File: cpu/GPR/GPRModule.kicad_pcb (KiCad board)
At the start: 2 copper layers, 100 x 80 mm, 52 parts, among them J1 Interconnect, U1 74HCT574, U10 74LS245, U11 74LS126, U2 74HCT574, U3 74LS245, U4 74LS245, U5 74LS245, U6 74LS245, U7 74LS245, U8 74LS245, U9 74LS245

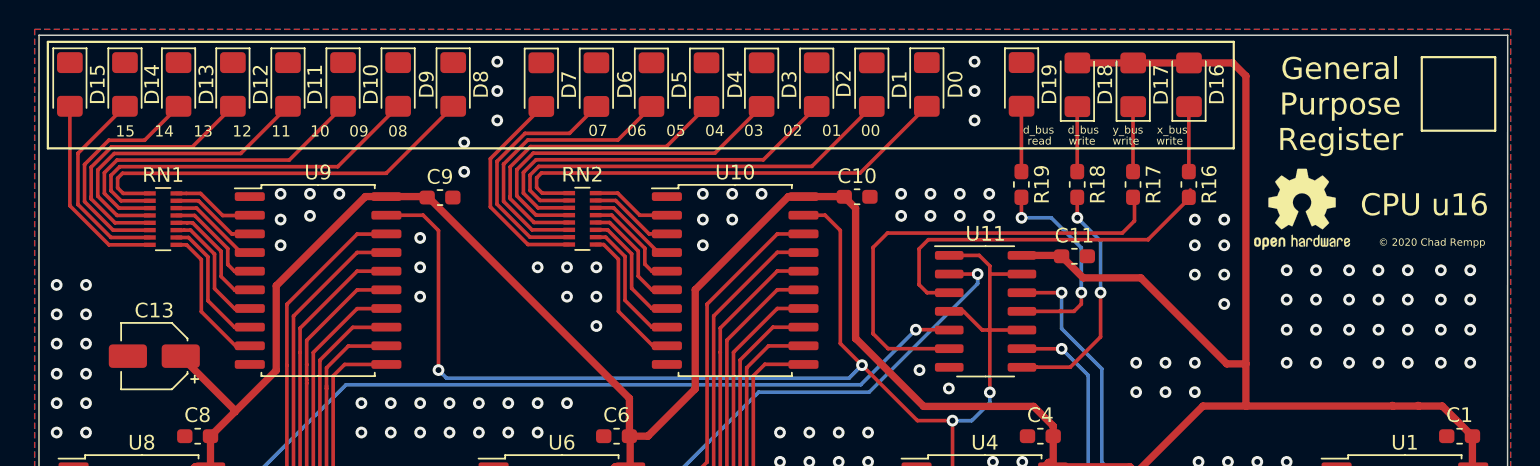
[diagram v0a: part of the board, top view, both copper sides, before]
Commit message: Fixed errors on GPR after testing board. * writing too small * stat LEDs not aligned * stat buffer needed CE to be active low - swapped 126 for a 125 * x_bus was backwards on the interconnect
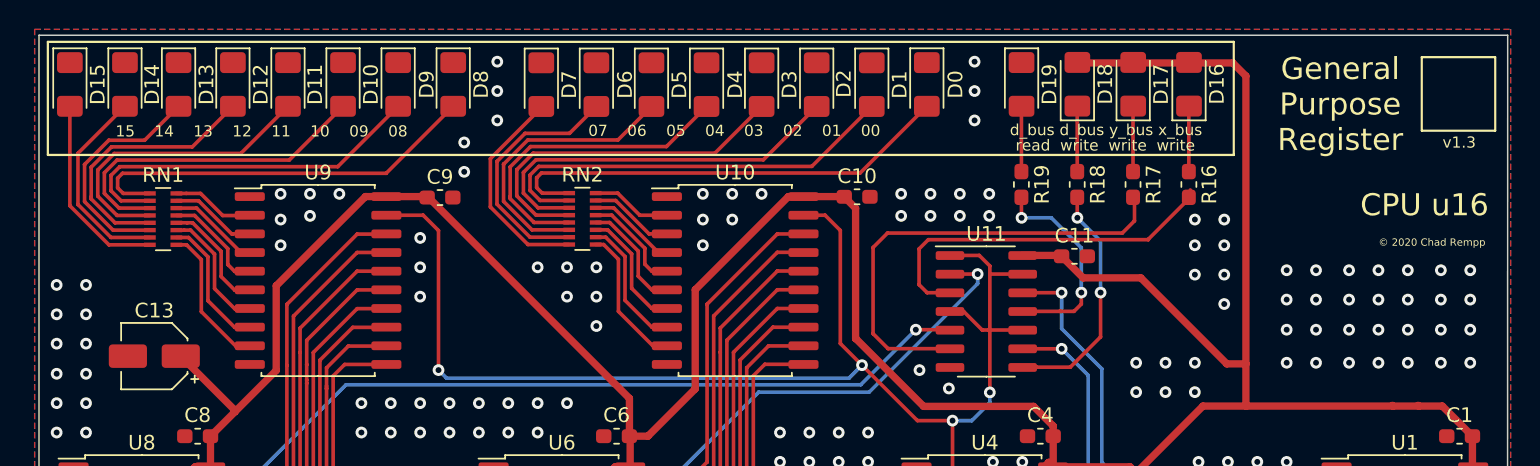
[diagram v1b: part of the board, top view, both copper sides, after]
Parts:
- removed REF**: OSHW-Logo2_7.3x6mm_SilkScreen, Symbol:OSHW-Logo2_7.3x6mm_SilkScreen
- U11: value 74LS126 -> 74LS125
- moved U11 0.05 mm to (156.3, 76.3)
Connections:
- J1 pad A34: /x_bus_00 -> /x_bus_15
- J1 pad A35: /x_bus_01 -> /x_bus_14
- J1 pad A36: /x_bus_02 -> /x_bus_13
- J1 pad A37: /x_bus_03 -> /x_bus_12
- J1 pad A38: /x_bus_04 -> /x_bus_11
- J1 pad A39: /x_bus_05 -> /x_bus_10
- J1 pad A40: /x_bus_06 -> /x_bus_09
- J1 pad A41: /x_bus_07 -> /x_bus_08
- J1 pad A42: /x_bus_08 -> /x_bus_07
- J1 pad A43: /x_bus_09 -> /x_bus_06
- J1 pad A44: /x_bus_10 -> /x_bus_05
- J1 pad A45: /x_bus_11 -> /x_bus_04
- J1 pad A46: /x_bus_12 -> /x_bus_03
- J1 pad A47: /x_bus_13 -> /x_bus_02
- J1 pad A48: /x_bus_14 -> /x_bus_01
- J1 pad A49: /x_bus_15 -> /x_bus_00
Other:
- board text added: "v1.3"

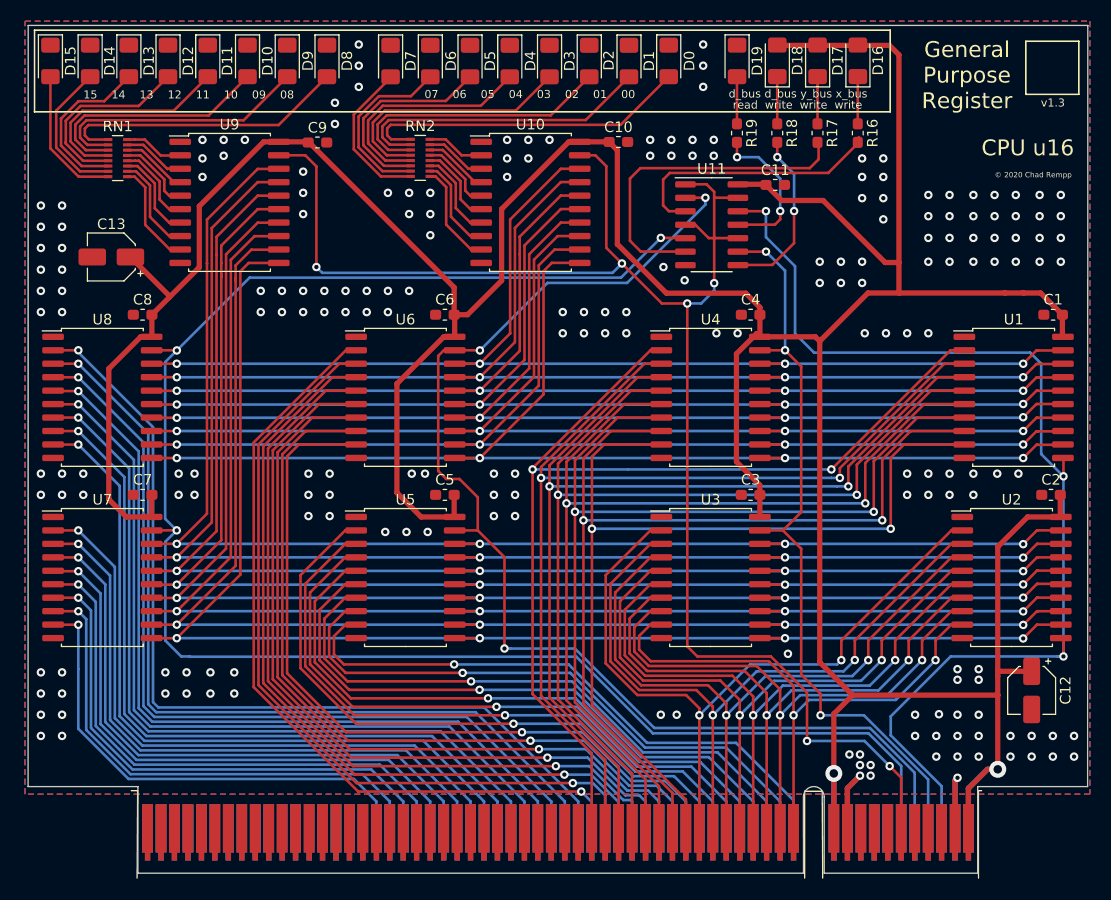
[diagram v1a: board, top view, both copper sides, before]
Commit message: V1.3 of GPR (fixed issues from first production board)
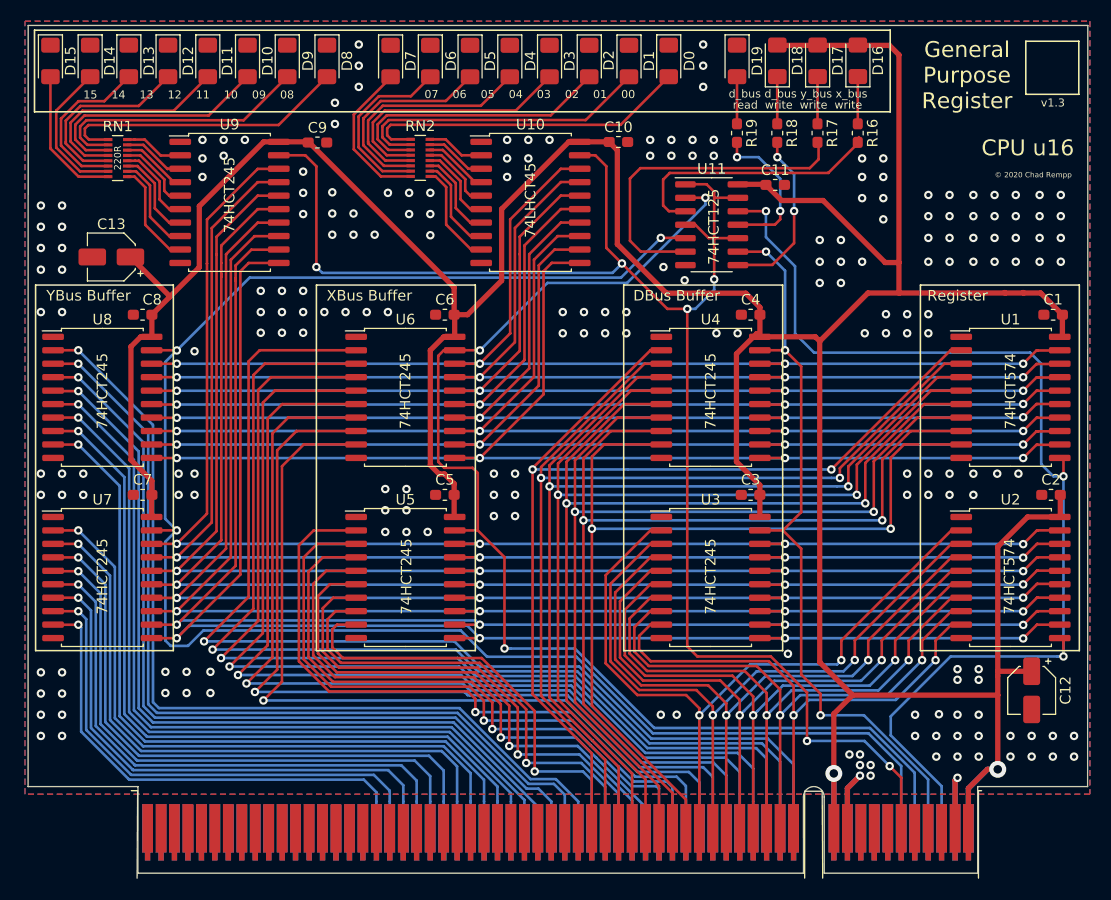
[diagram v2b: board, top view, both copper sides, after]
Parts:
- U10: value 74LS245 -> 74LHCT45
- U11: value 74LS125 -> 74HCT125
- U3, U4, U5, U6, U7, U8, U9: value 74LS245 -> 74HCT245
- moved U1 0.30 mm to (184.5, 92.6)
- moved U2 0.10 mm to (184.5, 109.6)
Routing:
- net /x_bus_00: track 77.9 -> 107.9 mm
- net /x_bus_01: track 77.9 -> 104.5 mm
- net /x_bus_02: track 77.1 -> 101.2 mm
- net /x_bus_03: track 76.8 -> 97.2 mm
- net /x_bus_04: track 76.4 -> 93.4 mm
- net /x_bus_15: track 58.6 -> 44.3 mm
- net /x_bus_05: track 76.0 -> 89.7 mm
- net /x_bus_14: track 59.3 -> 47.0 mm
- net +5V: track 392.3 -> 380.9 mm
- net /x_bus_13: track 60.1 -> 49.6 mm
- net /x_bus_06: track 75.7 -> 85.9 mm
- net /x_bus_12: track 60.8 -> 52.4 mm
- net /x_bus_07: track 75.3 -> 82.0 mm
- net /x_bus_11: track 61.6 -> 55.1 mm
- net /x_bus_10: track 62.3 -> 59.2 mm
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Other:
- board text added: "DBus Buffer"
- board text added: "Register"
- board text added: "XBus Buffer"
- board text added: "YBus Buffer"

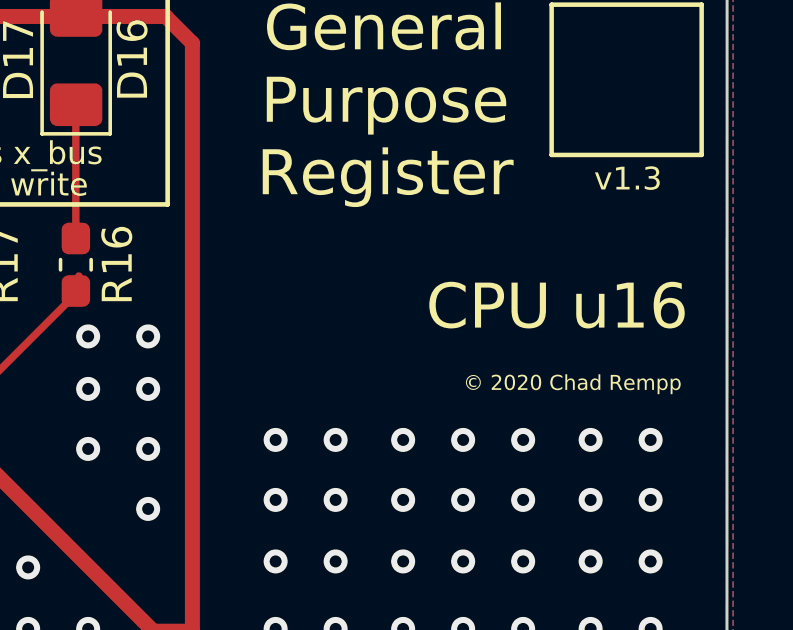
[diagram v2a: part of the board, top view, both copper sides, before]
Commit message: Finishing touches on GPR and Address Register
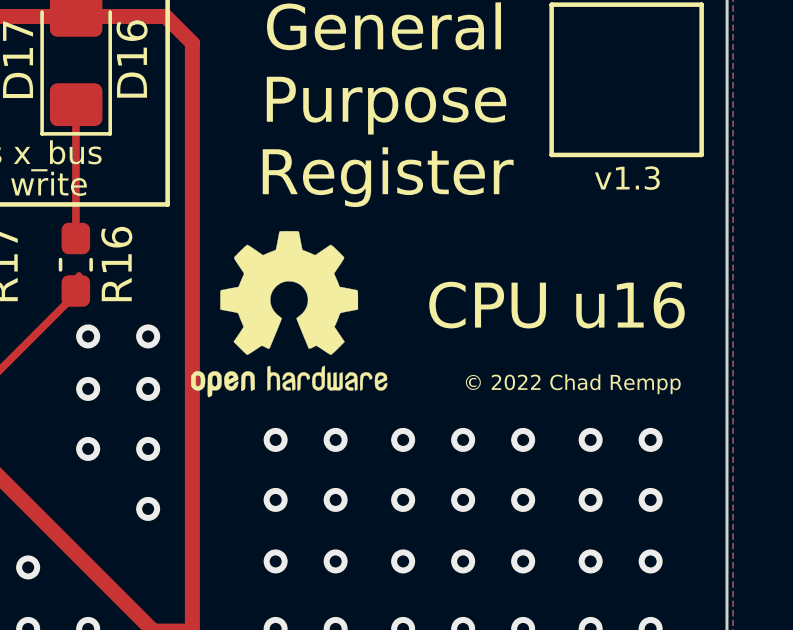
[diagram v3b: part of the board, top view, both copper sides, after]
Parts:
- added REF**: OSHW-Logo2_7.3x6mm_SilkScreen, Symbol:OSHW-Logo2_7.3x6mm_SilkScreen, F.Cu at (177.2, 69.3)
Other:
- board text added: "© 2022 Chad Rempp"
- board text removed: "© 2020 Chad Rempp"

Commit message: Upgrade to KiCad 6 and commit a bunch of random stuff
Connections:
- net /~DBG renamed /~{DBG}
- net /~d_bus_write renamed /~{d_bus_write}
- net /~x_bus_write renamed /~{x_bus_write}
- net /~y_bus_write renamed /~{y_bus_write}
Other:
- net class Default removed
- net class Power removed

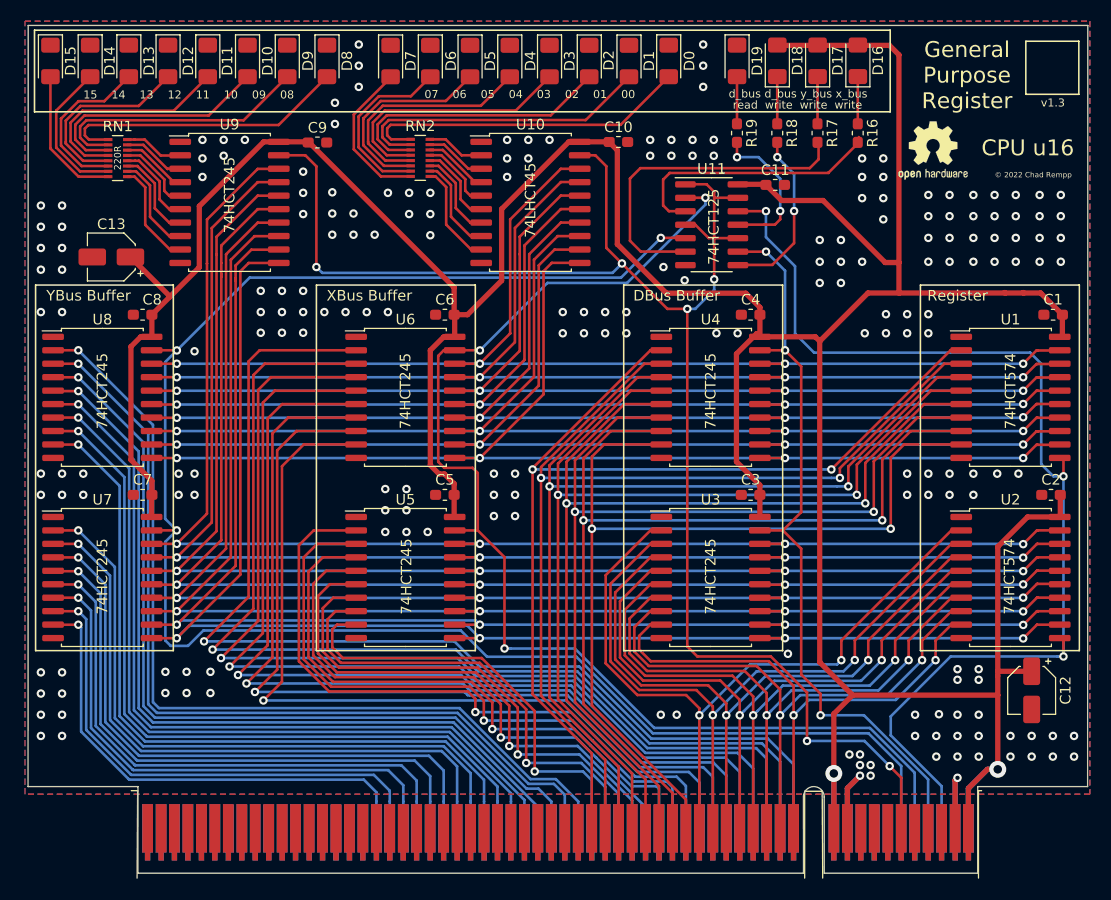
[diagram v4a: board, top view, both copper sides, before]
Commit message: GPR v1.4, removed old src, deleted a BOM
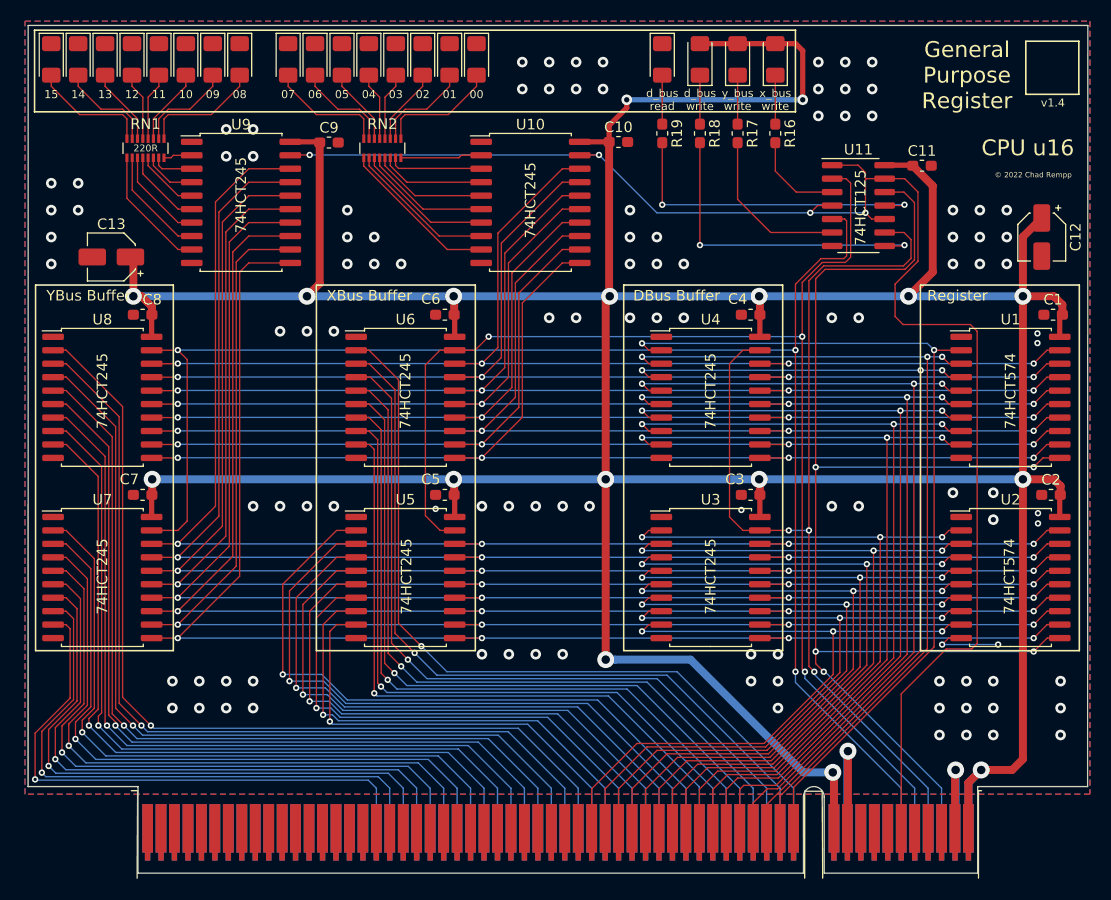
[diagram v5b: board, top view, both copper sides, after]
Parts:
- removed REF**: OSHW-Logo2_7.3x6mm_SilkScreen, Symbol:OSHW-Logo2_7.3x6mm_SilkScreen
- U10: value 74LHCT45 -> 74HCT245
- moved C12 42.8 mm to (187.5, 77.5)
- moved D0 18.1 mm to (134.1, 60.7)
- moved D1 16.9 mm to (131.6, 60.7)
- moved D2 15.7 mm to (129.0, 60.7)
- moved D3 14.5 mm to (126.5, 60.7)
- moved U11 14.0 mm to (170.1, 74.5)
- moved C11 14.0 mm to (176.1, 70.7)
- moved D4 13.3 mm to (124.0, 60.7)
- moved D5 12.1 mm to (121.4, 60.7)
- moved D6 10.9 mm to (118.9, 60.7)
- moved D7 9.67 mm to (116.3, 60.7)
- moved D8 8.24 mm to (111.8, 60.7)
- moved D16 7.80 mm to (162.3, 60.7)
- moved R16 7.78 mm to (162.3, 67.7)
- moved D17 7.55 mm to (158.8, 60.7)
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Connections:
- J1 pad A1: Net-(J1-PadA1) -> unconnected-(J1-PadA1)
- J1 pad A10: Net-(J1-PadA10) -> unconnected-(J1-PadA10)
- J1 pad A11: Net-(J1-PadA11) -> unconnected-(J1-PadA11)
- J1 pad A12: Net-(J1-PadA12) -> unconnected-(J1-PadA12)
- J1 pad A13: Net-(J1-PadA13) -> unconnected-(J1-PadA13)
- J1 pad A14: Net-(J1-PadA14) -> unconnected-(J1-PadA14)
- J1 pad A15: Net-(J1-PadA15) -> unconnected-(J1-PadA15)
- J1 pad A16: Net-(J1-PadA16) -> unconnected-(J1-PadA16)
- J1 pad A17: Net-(J1-PadA17) -> unconnected-(J1-PadA17)
- J1 pad A2: Net-(J1-PadA2) -> unconnected-(J1-PadA2)
- J1 pad A3: Net-(J1-PadA3) -> unconnected-(J1-PadA3)
- J1 pad A4: Net-(J1-PadA4) -> unconnected-(J1-PadA4)
- J1 pad A5: Net-(J1-PadA5) -> unconnected-(J1-PadA5)
- J1 pad A54: Net-(J1-PadA54) -> unconnected-(J1-PadA54)
- J1 pad A55: Net-(J1-PadA55) -> unconnected-(J1-PadA55)
- J1 pad A56: Net-(J1-PadA56) -> unconnected-(J1-PadA56)
- J1 pad A6: Net-(J1-PadA6) -> unconnected-(J1-PadA6)
- J1 pad A7: Net-(J1-PadA7) -> unconnected-(J1-PadA7)
- J1 pad A8: Net-(J1-PadA8) -> unconnected-(J1-PadA8)
- J1 pad A9: Net-(J1-PadA9) -> unconnected-(J1-PadA9)
- J1 pad B1: Net-(J1-PadB1) -> unconnected-(J1-PadB1)
- J1 pad B10: Net-(J1-PadB10) -> unconnected-(J1-PadB10)
- J1 pad B11: Net-(J1-PadB11) -> unconnected-(J1-PadB11)
- J1 pad B12: Net-(J1-PadB12) -> unconnected-(J1-PadB12)
- J1 pad B13: Net-(J1-PadB13) -> unconnected-(J1-PadB13)
- J1 pad B14: Net-(J1-PadB14) -> unconnected-(J1-PadB14)
- J1 pad B15: Net-(J1-PadB15) -> unconnected-(J1-PadB15)
- J1 pad B16: Net-(J1-PadB16) -> unconnected-(J1-PadB16)
- J1 pad B17: Net-(J1-PadB17) -> unconnected-(J1-PadB17)
- J1 pad B18: Net-(J1-PadB18) -> unconnected-(J1-PadB18)
- J1 pad B19: Net-(J1-PadB19) -> unconnected-(J1-PadB19)
- J1 pad B2: Net-(J1-PadB2) -> unconnected-(J1-PadB2)
- J1 pad B20: Net-(J1-PadB20) -> unconnected-(J1-PadB20)
- J1 pad B21: Net-(J1-PadB21) -> unconnected-(J1-PadB21)
- J1 pad B22: Net-(J1-PadB22) -> unconnected-(J1-PadB22)
- J1 pad B23: Net-(J1-PadB23) -> unconnected-(J1-PadB23)
- J1 pad B24: Net-(J1-PadB24) -> unconnected-(J1-PadB24)
- J1 pad B25: Net-(J1-PadB25) -> unconnected-(J1-PadB25)
- J1 pad B26: Net-(J1-PadB26) -> unconnected-(J1-PadB26)
- J1 pad B27: Net-(J1-PadB27) -> unconnected-(J1-PadB27)
- J1 pad B28: Net-(J1-PadB28) -> unconnected-(J1-PadB28)
- J1 pad B29: Net-(J1-PadB29) -> unconnected-(J1-PadB29)
- J1 pad B3: Net-(J1-PadB3) -> unconnected-(J1-PadB3)
- J1 pad B30: Net-(J1-PadB30) -> unconnected-(J1-PadB30)
- J1 pad B31: Net-(J1-PadB31) -> unconnected-(J1-PadB31)
- J1 pad B32: Net-(J1-PadB32) -> unconnected-(J1-PadB32)
- J1 pad B33: Net-(J1-PadB33) -> unconnected-(J1-PadB33)
- J1 pad B34: /d_bus_00 -> /d_bus_15
- J1 pad B35: /d_bus_01 -> /d_bus_14
- J1 pad B36: /d_bus_02 -> /d_bus_13
- J1 pad B37: /d_bus_03 -> /d_bus_12
- J1 pad B38: /d_bus_04 -> /d_bus_11
- J1 pad B39: /d_bus_05 -> /d_bus_10
- J1 pad B4: Net-(J1-PadB4) -> unconnected-(J1-PadB4)
- J1 pad B40: /d_bus_06 -> /d_bus_09
- J1 pad B41: /d_bus_07 -> /d_bus_08
- J1 pad B42: /d_bus_08 -> /d_bus_07
- J1 pad B43: /d_bus_09 -> /d_bus_06
- J1 pad B44: /d_bus_10 -> /d_bus_05
- J1 pad B45: /d_bus_11 -> /d_bus_04
- J1 pad B46: /d_bus_12 -> /d_bus_03
- J1 pad B47: /d_bus_13 -> /d_bus_02
- J1 pad B48: /d_bus_14 -> /d_bus_01
- J1 pad B49: /d_bus_15 -> /d_bus_00
- J1 pad B5: Net-(J1-PadB5) -> unconnected-(J1-PadB5)
- J1 pad B54: Net-(J1-PadB54) -> unconnected-(J1-PadB54)
- J1 pad B55: Net-(J1-PadB55) -> unconnected-(J1-PadB55)
- J1 pad B56: Net-(J1-PadB56) -> unconnected-(J1-PadB56)
- J1 pad B58: Net-(J1-PadB58) -> unconnected-(J1-PadB58)
- J1 pad B59: Net-(J1-PadB59) -> unconnected-(J1-PadB59)
- J1 pad B6: Net-(J1-PadB6) -> unconnected-(J1-PadB6)
- J1 pad B60: Net-(J1-PadB60) -> unconnected-(J1-PadB60)
- J1 pad B7: Net-(J1-PadB7) -> unconnected-(J1-PadB7)
- J1 pad B8: Net-(J1-PadB8) -> unconnected-(J1-PadB8)
- J1 pad B9: Net-(J1-PadB9) -> unconnected-(J1-PadB9)
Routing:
- net +5V: track 380.9 -> 434.3 mm, vias 2 -> 17
- net /x_bus_00: track 107.9 -> 75.6 mm
- net /x_bus_01: track 104.5 -> 73.9 mm
- net /x_bus_02: track 101.2 -> 72.1 mm
- net /x_bus_03: track 97.2 -> 70.3 mm
- net /x_bus_04: track 93.4 -> 68.5 mm
- net /x_bus_05: track 89.7 -> 66.7 mm
- net /~{y_bus_write}: track 169.9 -> 147.1 mm
- net /~{d_bus_write}: track 74.5 -> 97.3 mm
- net /x_bus_06: track 85.9 -> 64.9 mm
- net Net-(D0-Pad2): track 31.6 -> 11.3 mm
- net Net-(D1-Pad2): track 29.2 -> 9.30 mm
- net Net-(D2-Pad2): track 26.8 -> 7.26 mm
- net /x_bus_07: track 82.0 -> 63.2 mm
- net /d_bus_00: track 101.1 -> 83.1 mm
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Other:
- board text added: "00"
- board text added: "01"
- board text added: "02"
- board text added: "03"
- board text added: "04"
- board text added: "05"
- board text added: "06"
- board text added: "07"
- board text added: "08"
- board text added: "09"
- board text added: "10"
- board text added: "11"
- board text added: "12"
- board text added: "13"
- board text added: "14"
- board text added: "15"
- board text added: "d_bus read"
- board text added: "d_bus write"
- board text added: "v1.4"
- board text added: "x_bus write"
- board text added: "y_bus write"
- board text removed: "07 06 05 04 03 02 01 00"
- board text removed: "15 14 13 12 11 10 09 08"
- board text removed: "d_bus d_bus y_bus x_bus"
- board text removed: "read write write write"
- board text removed: "v1.3"
